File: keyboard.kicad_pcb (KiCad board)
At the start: 2 copper layers, 145 x 180.5 mm, 164 parts, among them P1 USB_OTG, P10 CONN_01X01, P11 CONN_01X01, P12 CONN_01X01, P13 CONN_01X01, P14 CONN_01X01, P15 CONN_01X06, P16 CONN_01X06, P17 CONN_01X01, P18 CONN_01X06, P2 CONN_02X03, P20 CONN_01X01, P3 CONN_01X01, P4 CONN_01X01, P5 CONN_01X01, P6 CONN_01X01, P7 CONN_01X01, P8 CONN_01X01, P9 CONN_01X01, SW1 SW_PUSH, SW10 SW_PUSH, SW11 SW_PUSH, SW12 SW_PUSH, SW13 SW_PUSH, SW14 SW_PUSH, SW15 SW_PUSH, SW16 SW_PUSH, SW2 SW_PUSH, SW24 SW_PUSH, SW25 SW_PUSH, SW26 SW_PUSH, SW27 SW_PUSH, SW28 SW_PUSH, SW29 SW_PUSH, SW3 SW_PUSH, SW30 SW_PUSH, SW31 SW_PUSH, SW32 SW_PUSH, SW33 SW_PUSH, SW34 SW_PUSH, SW35 SW_PUSH, SW36 SW_PUSH, SW37 SW_PUSH, SW4 SW_PUSH, SW5 SW_PUSH, SW6 SW_PUSH, SW7 SW_PUSH, SW8 SW_PUSH, SW9 SW_PUSH, U1 ATmega32U4, X1 CRYSTAL_SMD

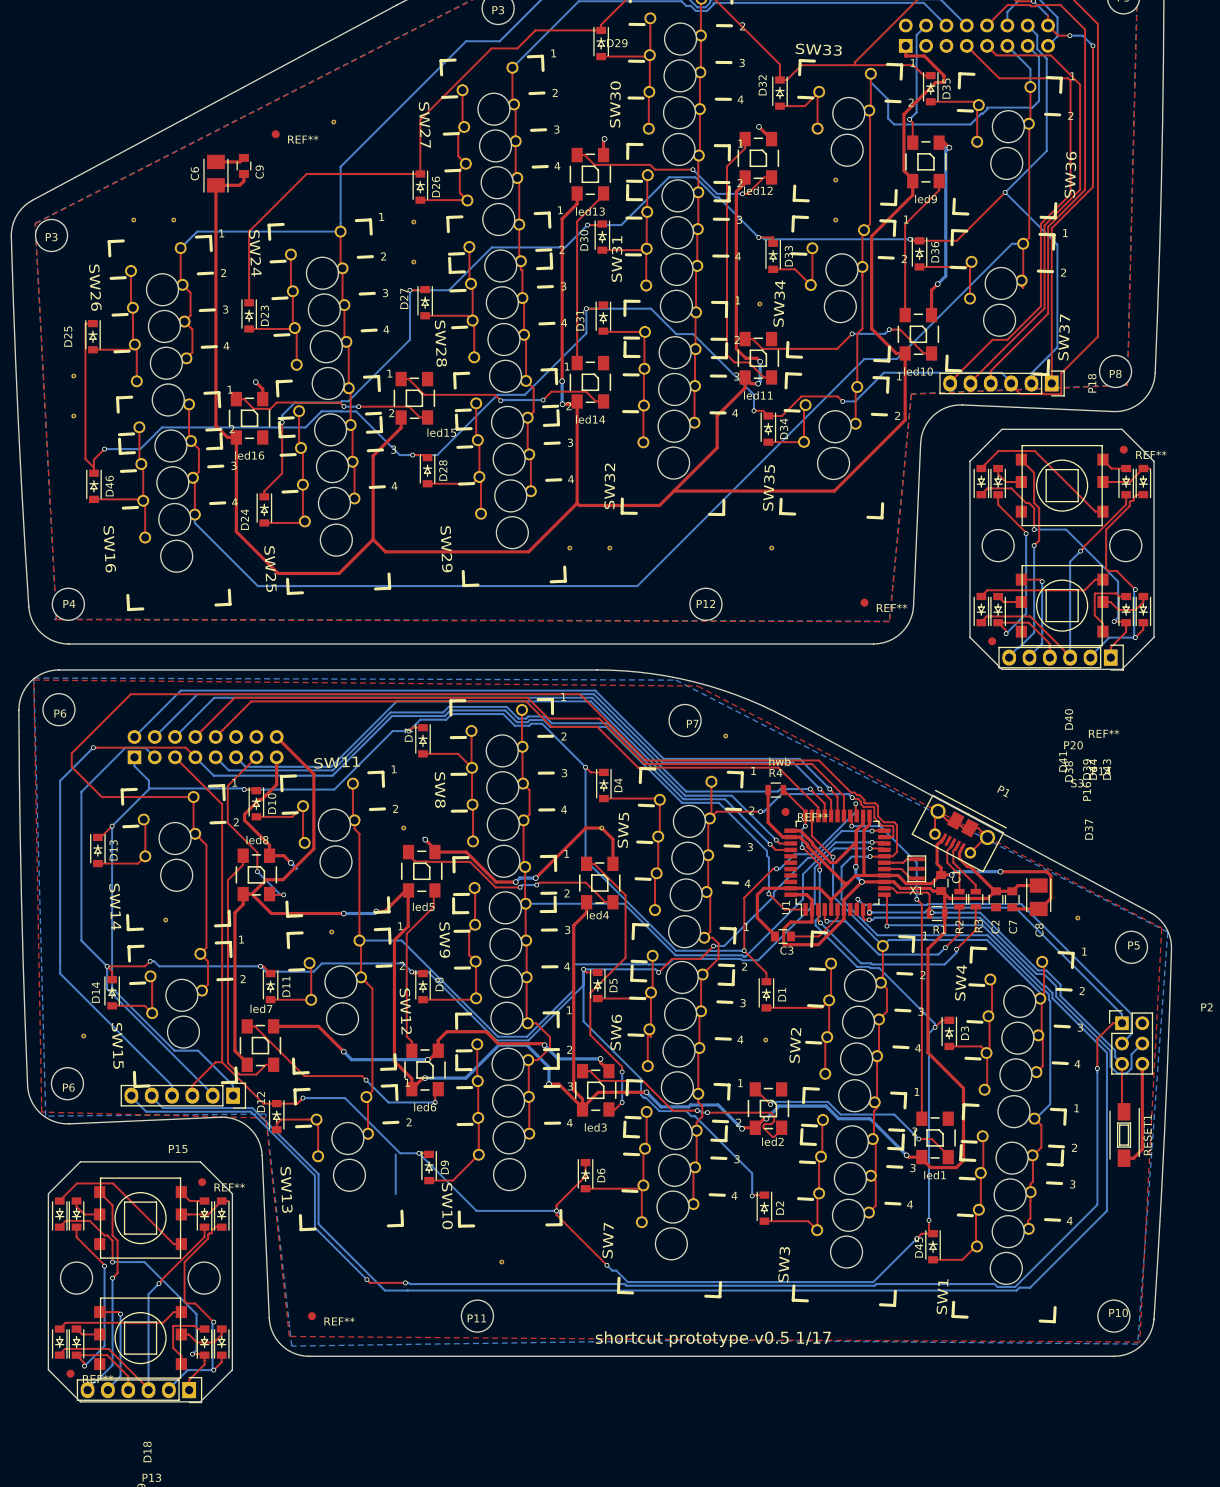
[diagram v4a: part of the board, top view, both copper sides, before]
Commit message: shortened thumbs, fid refs
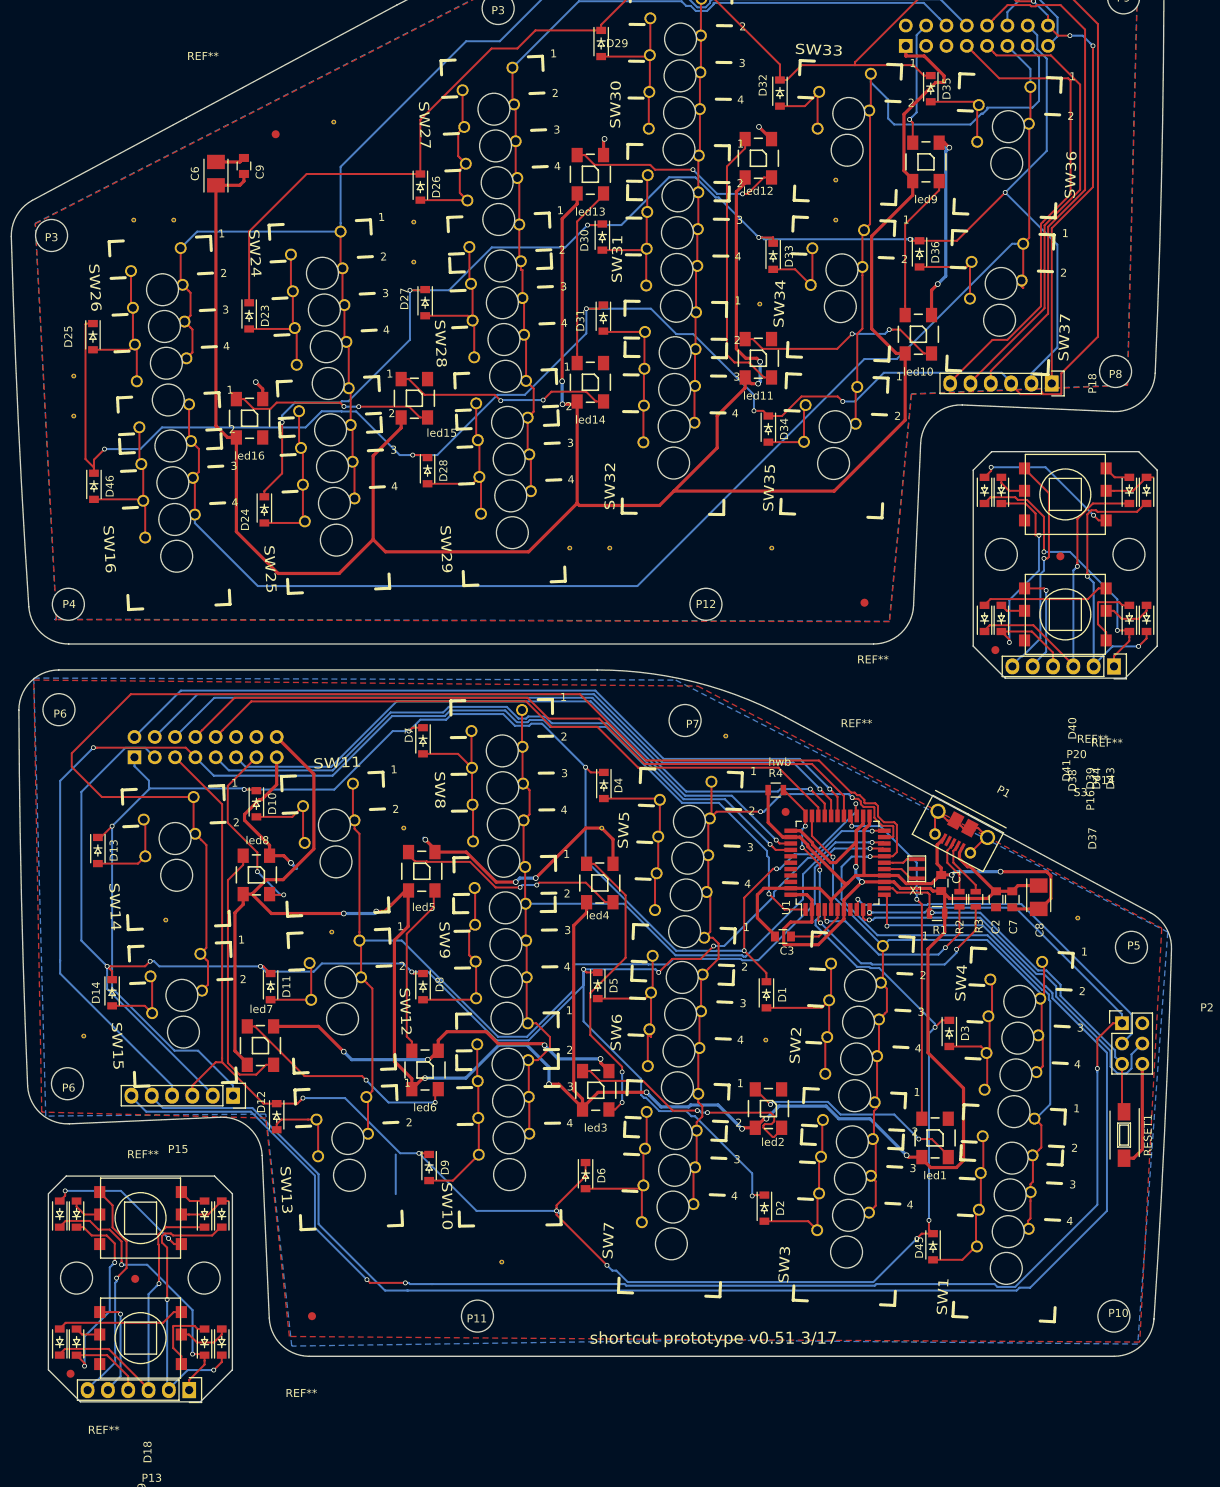
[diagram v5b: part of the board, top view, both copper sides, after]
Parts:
- moved REF** 15.5 mm to (153.1, 77.8)
- moved REF** 14.7 mm to (37.4, 168.1)
- moved D38 1.17 mm to (163.8, 85.5)
- moved D39 1.17 mm to (143.6, 85.5)
- moved D41 1.17 mm to (143.6, 69.5)
- moved D42 1.17 mm to (163.8, 69.5)
- moved P16 1.17 mm to (159.8, 91.5)
- moved P20 1.17 mm to (161.7, 77.5)
- moved D37 1.17 mm to (161.7, 85.5)
- moved D40 1.17 mm to (145.7, 85.5)
- moved D43 1.17 mm to (161.7, 69.5)
- moved D44 1.17 mm to (145.7, 69.5)
- moved P14 1.17 mm to (145.7, 77.5)
- moved S3 1.17 mm to (153.7, 85.0)
- moved S4 1.17 mm to (153.7, 70.0)
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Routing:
- net /right keys/thumb/row2: track 63.5 -> 74.0 mm
- net /right keys/thumb/row4: track 61.8 -> 67.5 mm
- net /right keys/thumb/row3: track 73.7 -> 79.3 mm
- net /right keys/thumb/col2: track 54.6 -> 56.5 mm
- net Net-(D19-Pad2): track 38.6 -> 37.6 mm, vias 0 -> 4
- net /right keys/thumb/row1: track 71.6 -> 70.9 mm
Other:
- outline, holes or cut-outs redrawn
- board text added: "shortcut prototype v0.51 3/17"
- board text removed: "shortcut prototype v0.5 1/17"

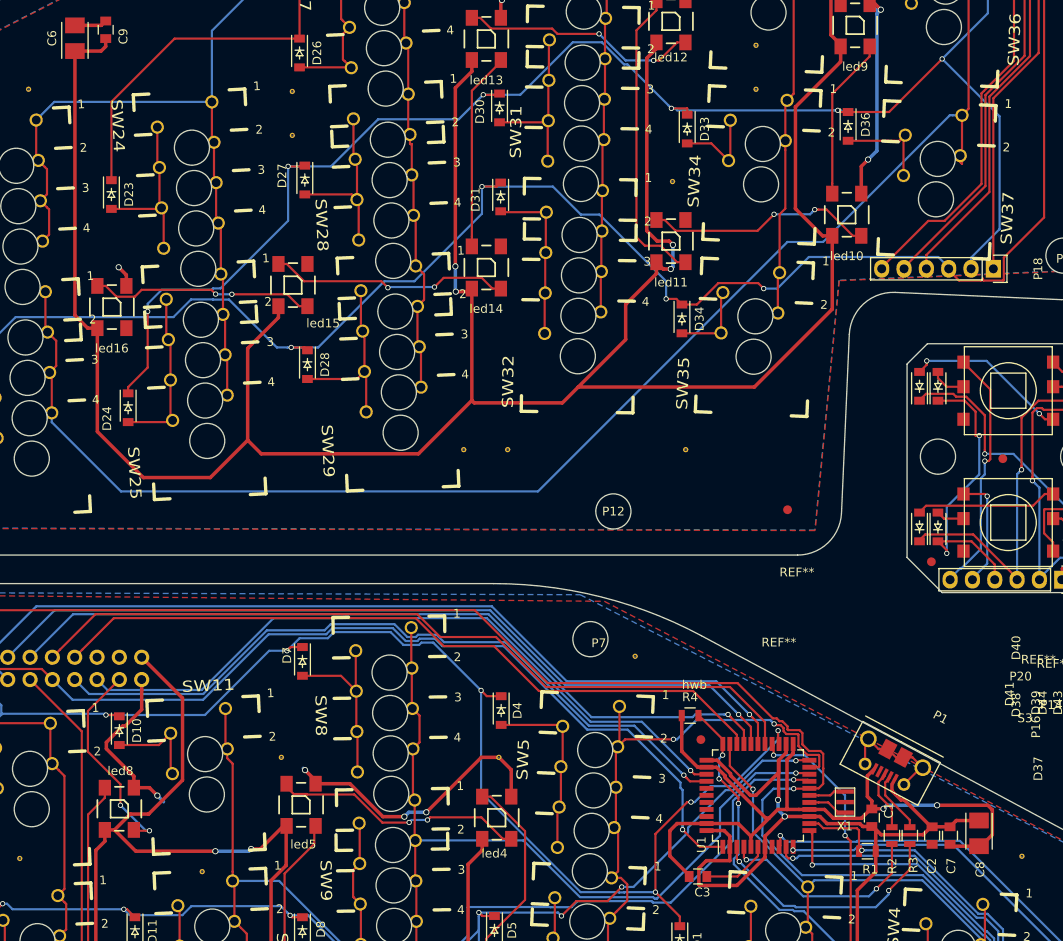
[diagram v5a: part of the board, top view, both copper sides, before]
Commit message: fix vias under pads, serial silks
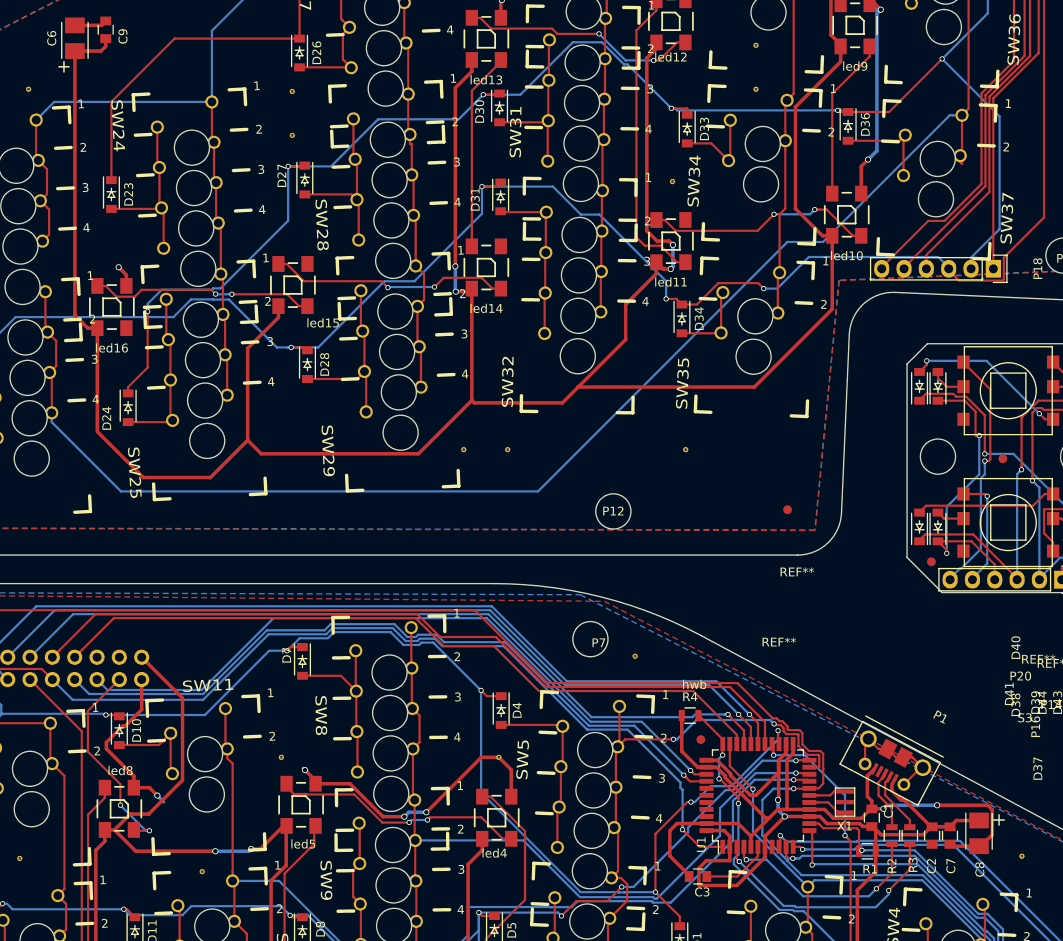
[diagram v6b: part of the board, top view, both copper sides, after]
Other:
- board text added: "+"

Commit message: changed size to a3 and moved boards
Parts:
- moved C1 70.4 mm to (194.7, 160.6)
- moved C2 70.4 mm to (201.5, 162.7)
- moved C3 70.4 mm to (174.9, 167.3)
- moved C7 70.4 mm to (203.6, 162.7)
- moved D1 70.4 mm to (172.8, 174.6)
- moved D14 70.4 mm to (91.0, 174.3)
- moved D16 70.4 mm to (104.8, 218.0)
- moved D17 70.4 mm to (84.5, 218.0)
- moved D19 70.4 mm to (84.5, 202.0)
- moved D2 70.4 mm to (172.6, 201.3)
- moved D20 70.4 mm to (104.8, 202.0)
- moved D24 70.4 mm to (110.1, 114.0)
- moved D27 70.4 mm to (130.2, 88.1)
- moved D28 70.4 mm to (130.5, 109.1)
- moved D29 70.4 mm to (152.2, 55.7)
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
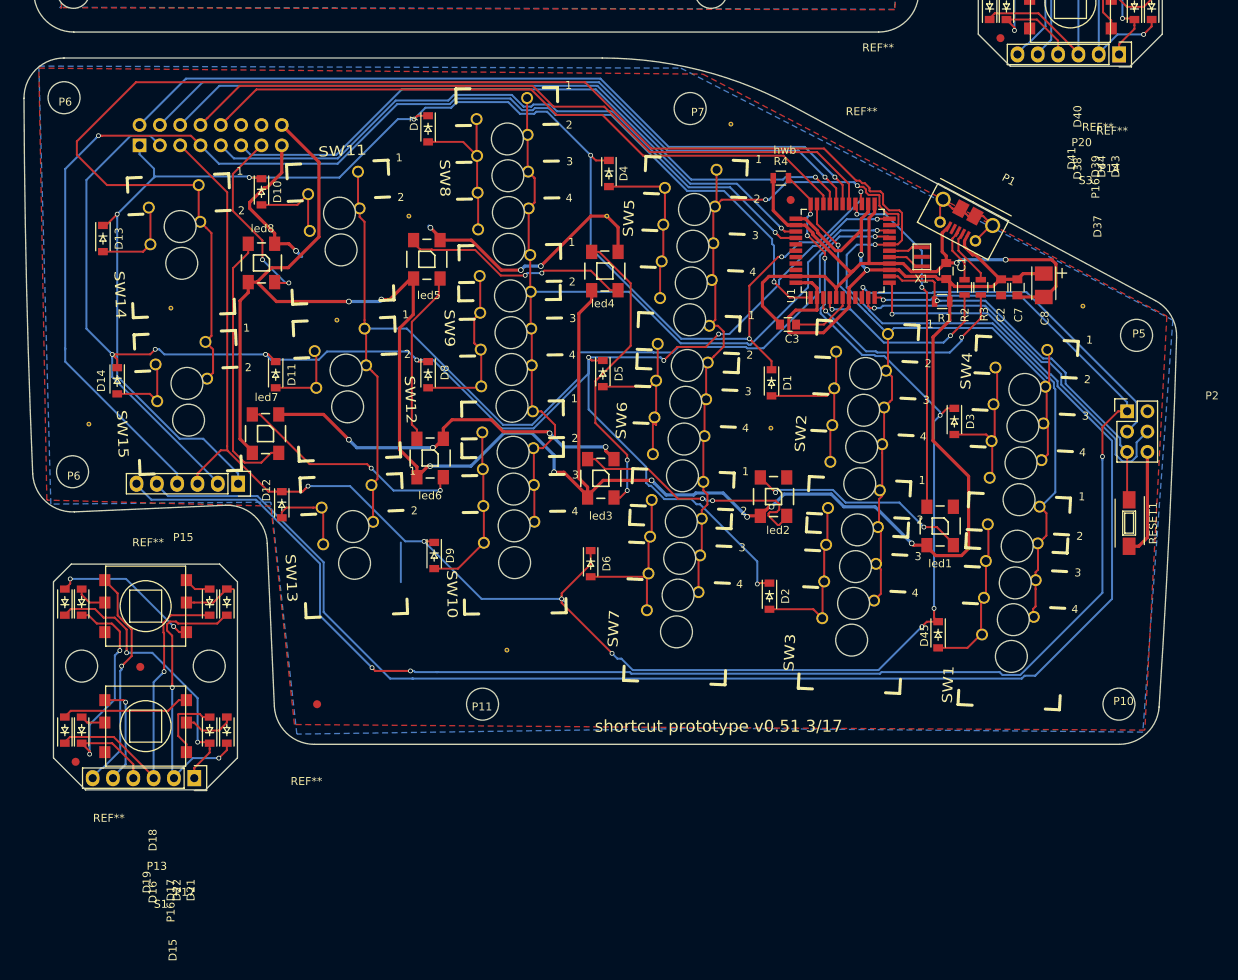
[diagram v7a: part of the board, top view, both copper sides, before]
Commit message: moved outlines
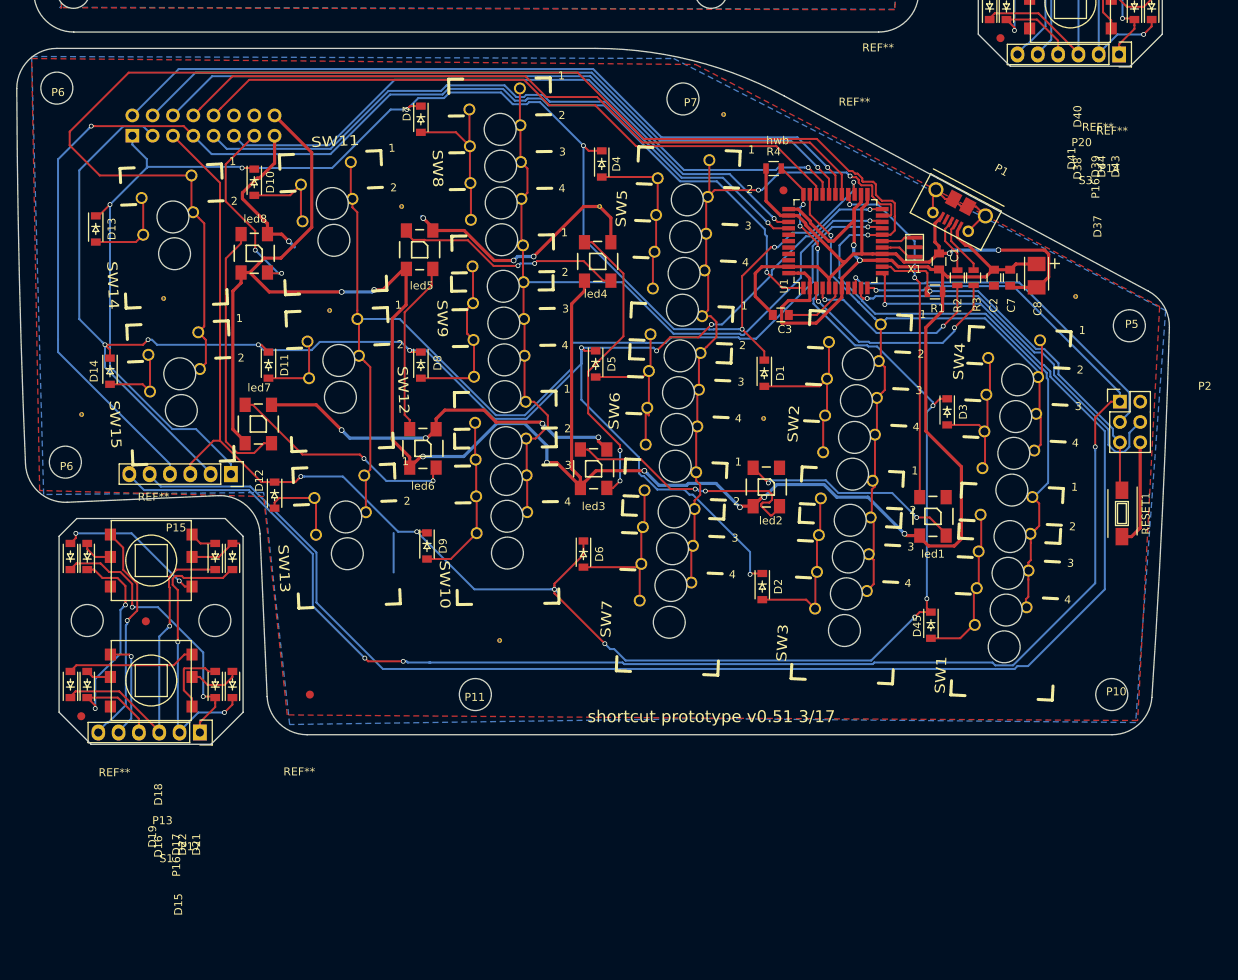
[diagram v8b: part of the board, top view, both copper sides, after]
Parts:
- moved REF** 5.74 mm to (86.5, 216.3)
- moved D16 5.74 mm to (105.5, 212.3)
- moved D17 5.74 mm to (85.2, 212.3)
- moved D19 5.74 mm to (85.2, 196.3)
- moved D20 5.74 mm to (105.5, 196.3)
- moved P13 5.74 mm to (103.2, 204.3)
- moved P17 5.74 mm to (87.3, 204.3)
- moved REF** 5.74 mm to (94.6, 204.4)
- moved D15 5.74 mm to (103.3, 212.3)
- moved D18 5.74 mm to (87.3, 212.3)
- moved D21 5.74 mm to (103.3, 196.3)
- moved D22 5.74 mm to (87.3, 196.3)
- moved P16 5.74 mm to (101.4, 218.3)
- moved S1 5.74 mm to (95.3, 211.8)
- moved S2 5.74 mm to (95.3, 196.8)
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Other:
- board size 145 x 180.5 mm -> 144.1 x 174.8 mm
